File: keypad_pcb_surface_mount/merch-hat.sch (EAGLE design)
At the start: 15 parts

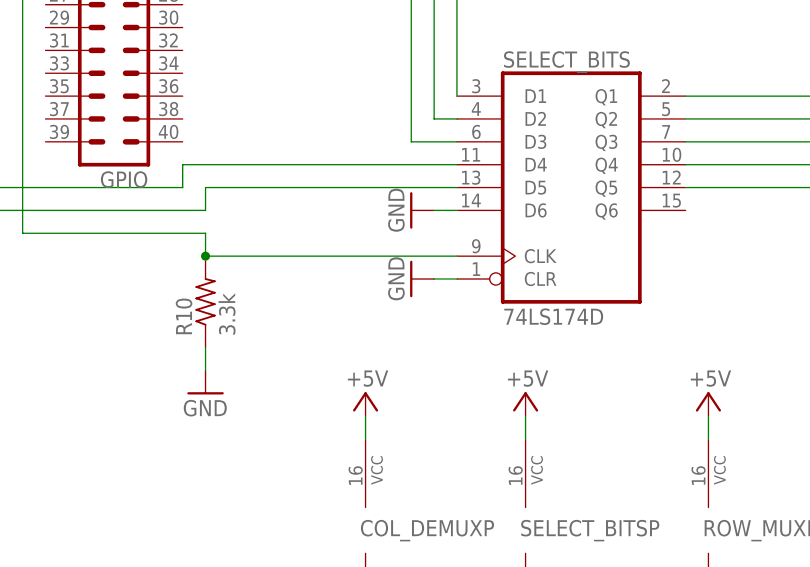
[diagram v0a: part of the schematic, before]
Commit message: update pcbs to remove clear bug on 74174 chip
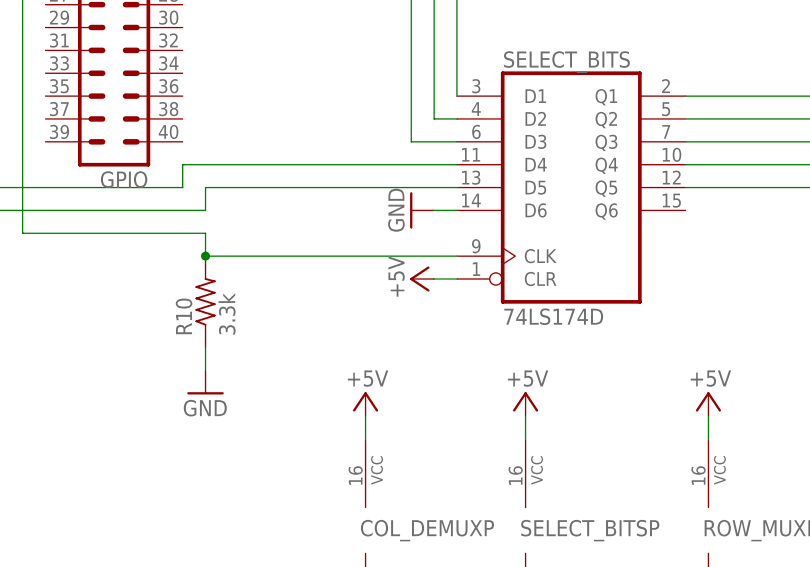
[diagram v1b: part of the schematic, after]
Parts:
- R1, R10, R2, R3, R4, R5, R6, R7, R8, R9: device resistor:R-US_R0402 -> resistor:R-US_R0805
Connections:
- net +5V: now also SELECT_BITSA.CLR
- net GND: no longer SELECT_BITSA.CLR
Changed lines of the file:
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@@
 <grid distance="0.1" unitdist="inch" unit="inch" style="lines" multiple="1" display="no" altdistance="0.01" altunitdist="inch" altunit="inch"/>
 <layers>
-<layer number="1" name="Top" color="4" fill="1" visible="no" active="no"/>
-<layer number="2" name="Route2" color="1" fill="3" visible="no" active="no"/>
-<layer number="3" name="Route3" color="4" fill="3" visible="no" active="no"/>
-<layer number="14" name="Route14" color="1" fill="6" visible="no" active="no"/>
-<layer number="15" name="Route15" color="4" fill="6" visible="no" active="no"/>
-<layer number="16" name="Bottom" color="1" fill="1" visible="no" active="no"/>
-<layer number="17" name="Pads" color="2" fill="1" visible="no" active="no"/>
-<layer number="18" name="Vias" color="2" fill="1" visible="no" active="no"/>
-<layer number="19" name="Unrouted" color="6" fill="1" visible="no" active="no"/>
-<layer number="20" name="Dimension" color="15" fill="1" visible="no" active="no"/>
-<layer number="21" name="tPlace" color="7" fill="1" visible="no" active="no"/>
-<layer number="22" name="bPlace" color="7" fill="1" visible="no" active="no"/>
-<layer number="23" name="tOrigins" color="15" fill="1" visible="no" active="no"/>
-<layer number="24" name="bOrigins" color="15" fill="1" visible="no" active="no"/>
-<layer number="25" name="tNames" color="7" fill="1" visible="no" active="no"/>
-<layer number="26" name="bNames" color="7" fill="1" visible="no" active="no"/>
-<layer number="27" name="tValues" color="7" fill="1" visible="no" active="no"/>
-<layer number="28" name="bValues" color="7" fill="1" visible="no" active="no"/>
+<layer number="1" name="Top" color="4" fill="1" visible="yes" active="no"/>
+<layer number="2" name="Route2" color="1" fill="3" visible="yes" active="no"/>
+<layer number="3" name="Route3" color="4" fill="3" visible="yes" active="no"/>
+<layer number="14" name="Route14" color="1" fill="6" visible="yes" active="no"/>
+<layer number="15" name="Route15" color="4" fill="6" visible="yes" active="no"/>
+<layer number="16" name="Bottom" color="1" fill="1" visible="yes" active="no"/>
+<layer number="17" name="Pads" color="2" fill="1" visible="yes" active="no"/>
+<layer number="18" name="Vias" color="2" fill="1" visible="yes" active="no"/>
+<layer number="19" name="Unrouted" color="6" fill="1" visible="yes" active="no"/>
+<layer number="20" name="Dimension" color="15" fill="1" visible="yes" active="no"/>
+<layer number="21" name="tPlace" color="7" fill="1" visible="yes" active="no"/>
+<layer number="22" name="bPlace" color="7" fill="1" visible="yes" active="no"/>
+<layer number="23" name="tOrigins" color="15" fill="1" visible="yes" active="no"/>
+<layer number="24" name="bOrigins" color="15" fill="1" visible="yes" active="no"/>
+<layer number="25" name="tNames" color="7" fill="1" visible="yes" active="no"/>
+<layer number="26" name="bNames" color="7" fill="1" visible="yes" active="no"/>
+<layer number="27" name="tValues" color="7" fill="1" visible="yes" active="no"/>
+<layer number="28" name="bValues" color="7" fill="1" visible="yes" active="no"/>
 <layer number="29" name="tStop" color="7" fill="3" visible="no" active="no"/>
 <layer number="30" name="bStop" color="7" fill="6" visible="no" active="no"/>
@@
 <layer number="35" name="tGlue" color="7" fill="4" visible="no" active="no"/>
 <layer number="36" name="bGlue" color="7" fill="5" visible="no" active="no"/>
-<layer number="37" name="tTest" color="7" fill="1" visible="no" active="no"/>
-<layer number="38" name="bTest" color="7" fill="1" visible="no" active="no"/>
+<layer number="37" name="tTest" color="7" fill="1" visible="yes" active="no"/>
+<layer number="38" name="bTest" color="7" fill="1" visible="yes" active="no"/>
 <layer number="39" name="tKeepout" color="4" fill="11" visible="no" active="no"/>
 <layer number="40" name="bKeepout" color="1" fill="11" visible="no" active="no"/>
@@
 <layer number="44" name="Drills" color="7" fill="1" visible="no" active="no"/>
 <layer number="45" name="Holes" color="7" fill="1" visible="no" active="no"/>
-<layer number="46" name="Milling" color="3" fill="1" visible="no" active="no"/>
-<layer number="47" name="Measures" color="7" fill="1" visible="no" active="no"/>
-<layer number="48" name="Document" color="7" fill="1" visible="no" active="no"/>
-<layer number="49" name="Reference" color="7" fill="1" visible="no" active="no"/>
-<layer number="50" name="dxf" color="7" fill="1" visible="no" active="no"/>
-<layer number="51" name="tDocu" color="7" fill="1" visible="no" active="no"/>
-<layer number="52" name="bDocu" color="7" fill="1" visible="no" active="no"/>
-<layer number="53" name="tGND_GNDA" color="7" fill="1" visible="no" active="no"/>
-<layer number="54" name="bGND_GNDA" color="7" fill="1" visible="no" active="no"/>
-<layer number="56" name="wert" color="7" fill="1" visible="no" active="no"/>
+<layer number="46" name="Milling" color="3" fill="1" visible="yes" active="no"/>
+<layer number="47" name="Measures" color="7" fill="1" visible="yes" active="no"/>
+<layer number="48" name="Document" color="7" fill="1" visible="yes" active="no"/>
+<layer number="49" name="Reference" color="7" fill="1" visible="yes" active="no"/>
+<layer number="50" name="dxf" color="7" fill="1" visible="yes" active="no"/>
+<layer number="51" name="tDocu" color="7" fill="1" visible="yes" active="no"/>
+<layer number="52" name="bDocu" color="7" fill="1" visible="yes" active="no"/>
+<layer number="53" name="tGND_GNDA" color="7" fill="1" visible="yes" active="no"/>
+<layer number="54" name="bGND_GNDA" color="7" fill="1" visible="yes" active="no"/>
+<layer number="56" name="wert" color="7" fill="1" visible="yes" active="no"/>
 <layer number="91" name="Nets" color="2" fill="1" visible="yes" active="yes"/>
 <layer number="92" name="Busses" color="1" fill="1" visible="yes" active="yes"/>
@@
 <part name="SELECT_BITS" library="74xx-us" deviceset="74*174" device="D" technology="LS" value="74LS174D"/>
 <part name="JP1" library="pinhead" deviceset="PINHD-1X10" device="" value="HEADER"/>
-<part name="R1" library="resistor" deviceset="R-US_" device="R0402" value="3.3k"/>
-<part name="R2" library="resistor" deviceset="R-US_" device="R0402" value="3.3k"/>
-<part name="R3" library="resistor" deviceset="R-US_" device="R0402" value="3.3k"/>
-<part name="R4" library="resistor" deviceset="R-US_" device="R0402" value="3.3k"/>
-<part name="R5" library="resistor" deviceset="R-US_" device="R0402" value="3.3k"/>
-<part name="R6" library="resistor" deviceset="R-US_" device="R0402" value="3.3k"/>
-<part name="R7" library="resistor" deviceset="R-US_" device="R0402" value="3.3k"/>
-<part name="R8" library="resistor" deviceset="R-US_" device="R0402" value="3.3k"/>
-<part name="R9" library="resistor" deviceset="R-US_" device="R0402" value="3.3k"/>
+<part name="R1" library="resistor" deviceset="R-US_" device="R0805" value="3.3k"/>
+<part name="R2" library="resistor" deviceset="R-US_" device="R0805" value="3.3k"/>
+<part name="R3" library="resistor" deviceset="R-US_" device="R0805" value="3.3k"/>
+<part name="R4" library="resistor" deviceset="R-US_" device="R0805" value="3.3k"/>
+<part name="R5" library="resistor" deviceset="R-US_" device="R0805" value="3.3k"/>
+<part name="R6" library="resistor" deviceset="R-US_" device="R0805" value="3.3k"/>
+<part name="R7" library="resistor" deviceset="R-US_" device="R0805" value="3.3k"/>
+<part name="R8" library="resistor" deviceset="R-US_" device="R0805" value="3.3k"/>
+<part name="R9" library="resistor" deviceset="R-US_" device="R0805" value="3.3k"/>
 <part name="P+3" library="supply1" deviceset="+5V" device=""/>
 <part name="GND1" library="supply1" deviceset="GND" device=""/>
 <part name="GND2" library="supply1" deviceset="GND" device=""/>
-<part name="GND3" library="supply1" deviceset="GND" device=""/>
 <part name="P+2" library="supply1" deviceset="+5V" device=""/>
 <part name="P+4" library="supply1" deviceset="+5V" device=""/>
@@
 <part name="GND4" library="supply1" deviceset="GND" device=""/>
 <part name="GND8" library="supply1" deviceset="GND" device=""/>
-<part name="R10" library="resistor" deviceset="R-US_" device="R0402" value="3.3k"/>
+<part name="R10" library="resistor" deviceset="R-US_" device="R0805" value="3.3k"/>
 <part name="GND9" library="supply1" deviceset="GND" device=""/>
+<part name="P+9" library="supply1" deviceset="+5V" device=""/>
 </parts>
 <sheets>
@@
 <instance part="GND1" gate="1" x="132.08" y="127" rot="R180"/>
 <instance part="GND2" gate="1" x="73.66" y="129.54" rot="R270"/>
-<instance part="GND3" gate="1" x="73.66" y="121.92" rot="R270"/>
 <instance part="P+2" gate="1" x="144.78" y="127" smashed="yes">
 <attribute name="VALUE" x="147.32" y="129.54" size="1.778" layer="96" rot="R180"/>
@@
 <instance part="R10" gate="G$1" x="50.8" y="119.38" rot="R90"/>
 <instance part="GND9" gate="1" x="50.8" y="109.22"/>
+<instance part="P+9" gate="1" x="73.66" y="121.92" smashed="yes" rot="R90">
+<attribute name="VALUE" x="71.12" y="124.46" size="1.778" layer="96" rot="R270"/>
+</instance>
 </instances>
 <busses>
@@
 <pinref part="GND2" gate="1" pin="GND"/>
 <wire x1="78.74" y1="129.54" x2="76.2" y2="129.54" width="0.1524" layer="91"/>
-</segment>
-<segment>
-<pinref part="SELECT_BITS" gate="A" pin="CLR"/>
-<pinref part="GND3" gate="1" pin="GND"/>
-<wire x1="78.74" y1="121.92" x2="76.2" y2="121.92" width="0.1524" layer="91"/>
 </segment>
 <segment>
@@
 <wire x1="106.68" y1="106.68" x2="106.68" y2="104.14" width="0.1524" layer="91"/>
 </segment>
+<segment>
+<pinref part="SELECT_BITS" gate="A" pin="CLR"/>
+<wire x1="78.74" y1="121.92" x2="76.2" y2="121.92" width="0.1524" layer="91"/>
+<pinref part="P+9" gate="1" pin="+5V"/>
+</segment>
 </net>
